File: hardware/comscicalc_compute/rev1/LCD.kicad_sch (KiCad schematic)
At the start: 37 parts, among them IC4 FT811Q-T, J4 4-1734839-0, Y2 X1G004171001800

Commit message: Made yet another revision of the hardware using the rp2040
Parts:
- removed R25, R26, R27, R28, R29, R30, R31, R32, R33, R34, R35, R36, R38, R39, R40, R41, R42, R43, R44, R45, R46, R47, R48: 33R, Resistor_SMD:R_0402_1005Metric, symbol Device:R_Small
- removed R37: 0R, Resistor_SMD:R_0402_1005Metric, symbol Device:R_Small
- removed TP8: TestPoint, TestPoint:TestPoint_Pad_D1.5mm, symbol Connector:TestPoint
- Y2: value X1G004171001800 -> ECS-2520MV-120-BN-TR
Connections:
- net B2: now also IC4.35 (B2)
- net B3: now also IC4.34 (B3)
- net B4: now also IC4.33 (B4)
- net B5: now also IC4.32 (B5)
- net B6: now also IC4.31 (B6)
- net B7: now also IC4.30 (B7)
- net BACKLIGHT_PWM: now also IC4.24 (BACKLIGHT)
- net DE: now also IC4.25 (DE)
- net DISP: now also IC4.28 (DISP)
- net G2: now also IC4.42 (G2)
- net G3: now also IC4.41 (G3)
- net G4: now also IC4.40 (G4)
- net G5: now also IC4.39 (G5)
- net G6: now also IC4.38 (G6)
- net G7: now also IC4.37 (G7)
- net HSYNC: now also IC4.27 (HSYNC)
- net PCLK: now also IC4.29 (PCLK)
- net R2: now also IC4.48 (R2)
- net R3: now also IC4.47 (R3)
- net R4: now also IC4.46 (R4)
- net R5: now also IC4.45 (R5)
- net R6: now also IC4.44 (R6)
- net R7: now also IC4.43 (R7)
- net VSYNC: now also IC4.26 (VSYNC)

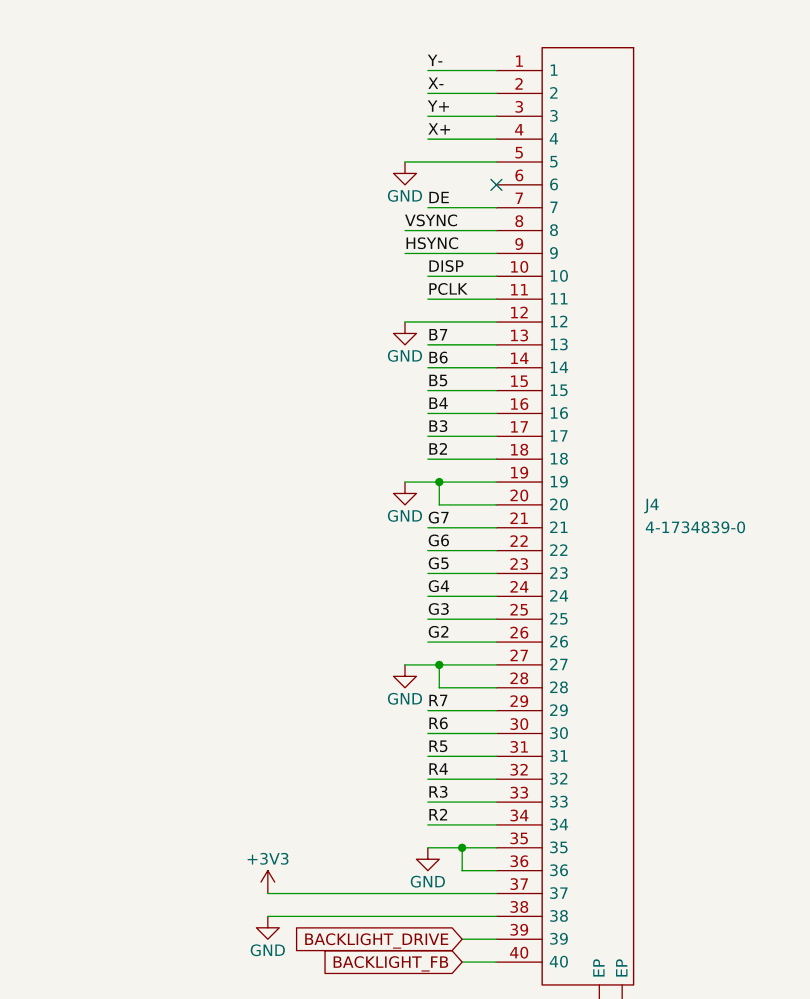
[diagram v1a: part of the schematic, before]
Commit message: Added hardware changes and some of the missing fonts
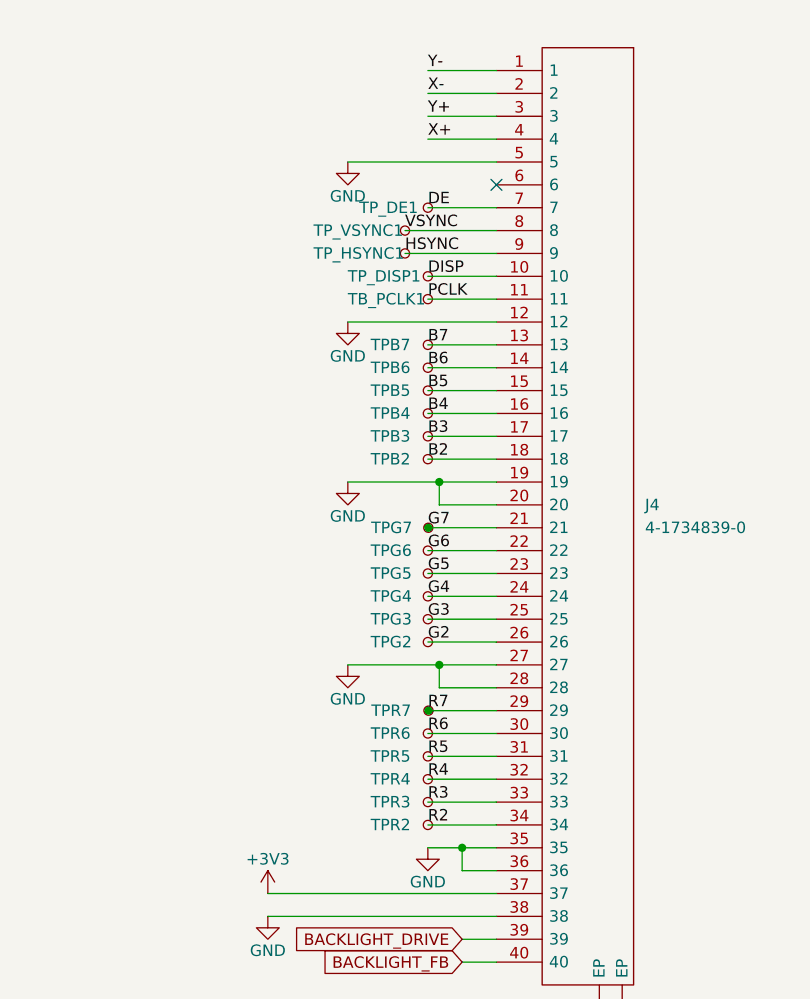
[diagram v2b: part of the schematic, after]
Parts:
- added TB_PCLK1, TPB2, TPB3, TPB4, TPB5, TPB6, TPB7, TPG2, TPG3, TPG4, TPG5, TPG6, TPG7, TPR2, TPR3, TPR4, TPR5, TPR6, TPR7, TP_DE1, TP_DISP1, TP_HSYNC1, TP_VSYNC1: TestPoint_Small, TestPoint:TestPoint_Pad_1.0x1.0mm, symbol Connector:TestPoint_Small
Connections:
- net B2: now also TPB2.1
- net B3: now also TPB3.1
- net B4: now also TPB4.1
- net B5: now also TPB5.1
- net B6: now also TPB6.1
- net B7: now also TPB7.1
- net DE: now also TP_DE1.1
- net DISP: now also TP_DISP1.1
- net G2: now also TPG2.1
- net G3: now also TPG3.1
- net G4: now also TPG4.1
- net G5: now also TPG5.1
- net G6: now also TPG6.1
- net G7: now also TPG7.1
- net HSYNC: now also TP_HSYNC1.1
- net PCLK: now also TB_PCLK1.1
- net R2: now also TPR2.1
- net R3: now also TPR3.1
- net R4: now also TPR4.1
- net R5: now also TPR5.1
- net R6: now also TPR6.1
- net R7: now also TPR7.1
- net VSYNC: now also TP_VSYNC1.1
